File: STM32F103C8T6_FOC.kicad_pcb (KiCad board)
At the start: 4 copper layers, 42.3 x 42.3 mm, 80 parts, among them IC1 BD9E303EFJ-LBE2, IC2 AS5600-ASOT, J1 USB_C_Receptacle_USB2.0_16P, J2 Conn_01x02_Socket, J3 Conn_01x04_Pin, J4 Conn_01x02_Socket, J5 Conn_01x04_Pin, J6 Conn_01x02_Socket, U2 SN65HVD230DR, U3 USBLC6-2SC6, U4 M24C64-RMN6TP, U5 TMC2209-LA, Y1 Crystal_16MHz

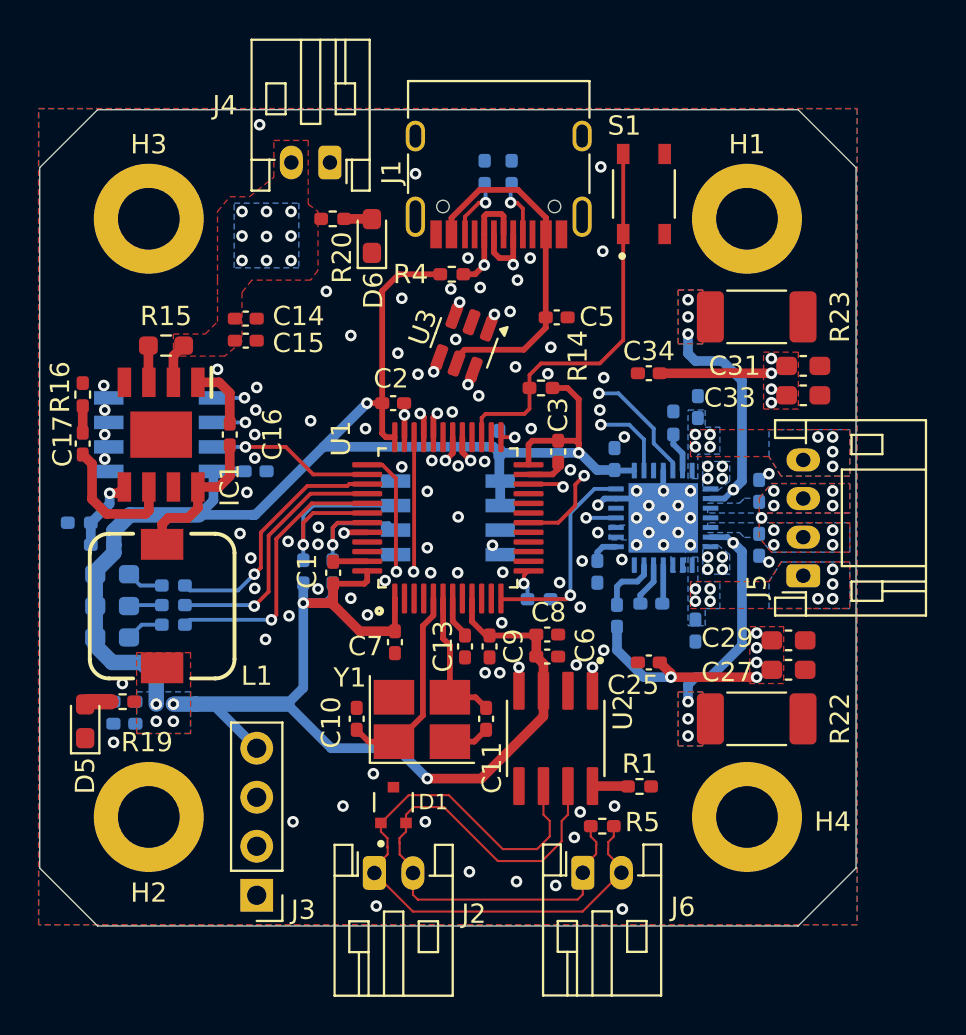
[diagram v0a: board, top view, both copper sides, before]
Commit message: Schematic check, Text adjustment & QoL changes
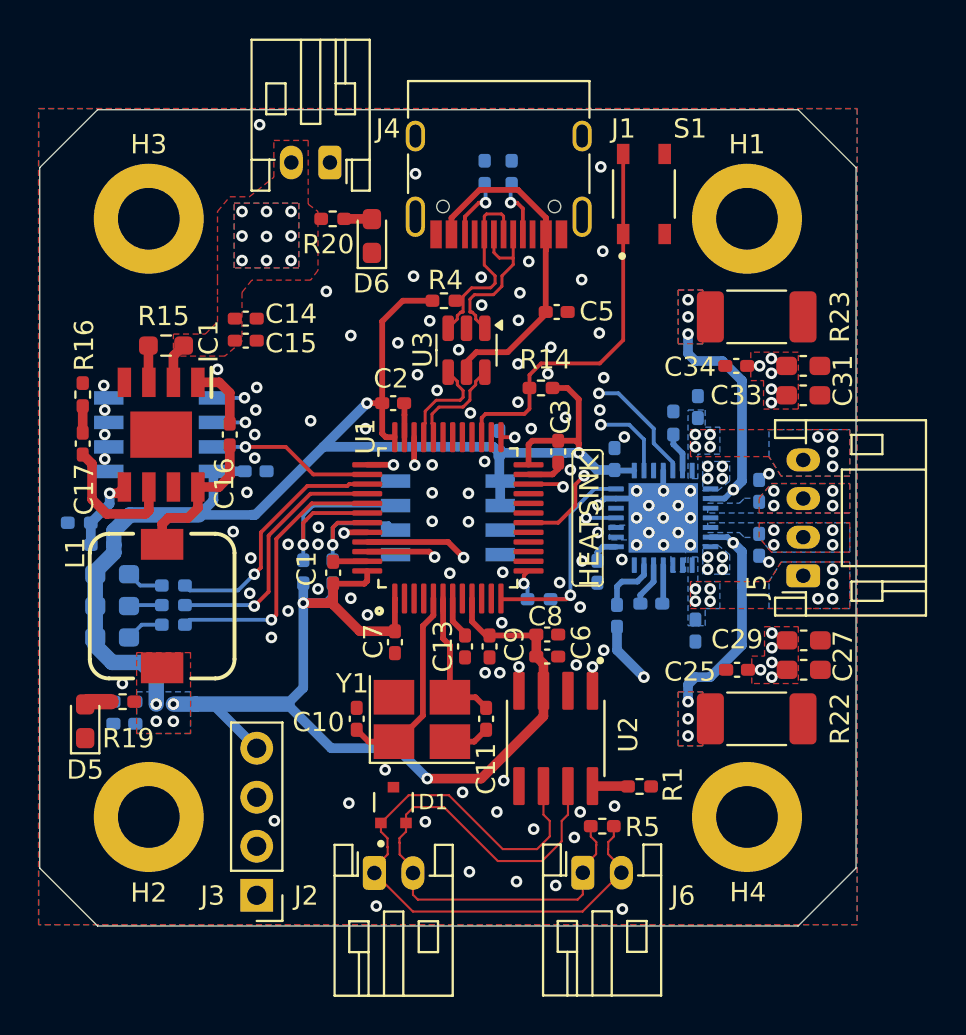
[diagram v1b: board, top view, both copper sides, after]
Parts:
- C27, C29, C31, C33: value 10uF -> 47uF
- moved C25 4.59 mm to (167.5, 108.2)
- moved C34 4.55 mm to (167.5, 92.5)
- moved R4 1.43 mm to (152.3, 89.1)
- moved C27 0.79 mm to (171.0, 108.2)
- moved C29 0.79 mm to (171.0, 106.7)
- moved U3 0.40 mm to (153.5, 91.6), turned to -90 degrees
- moved C5 0.28 mm to (158.2, 89.7)
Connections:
- U1 pad 29: /CAN_TX -> unconnected-(U1-PA8-Pad29)
- U1 pad 30: /CAN_RX -> unconnected-(U1-PA9-Pad30)
- U1 pad 45: unconnected-(U1-PB8-Pad45) -> /CAN_TX
- U1 pad 46: unconnected-(U1-PB9-Pad46) -> /CAN_RX
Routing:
- net +12V: track 77.7 -> 65.1 mm, vias 26 -> 28
- net /CAN_TX: track 18.7 -> 16.2 mm
- net /CAN_RX: track 15.8 -> 13.6 mm
- net +3.3V: track 126.6 -> 124.7 mm
- net /MCU_Peripherals/USB2_D-: track 7.46 -> 8.82 mm, vias 2 -> 0
- net /MCU_Peripherals/USB2_D+: track 10.4 -> 9.73 mm, vias 2 -> 0
- net /USB0_D+: track 4.63 -> 5.26 mm, vias 2 -> 0
- net Net-(U3-VBUS): track 18.2 -> 17.6 mm
- net /USB0_D-: track 5.40 -> 5.26 mm, vias 2 -> 0
- net GND: vias 104 -> 105
- added copper zone on In2.Cu, net +12V
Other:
- board text added: "3.3V"
- board text added: "B2 B1 A1 A2"
- board text added: "CLK"
- board text added: "DIO"
- board text added: "GND"
- board text added: "GND 12V"
- board text added: "H-L"
- board text added: "HEATSINK"
- board text added: "JLCJLCJLCJLC"
- board text added: "L-H"

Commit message: Constrains & Check
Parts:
- C10, C11: value C -> 30pF; footprint Capacitor_SMD:C_0402_1005Metric_Pad0.74x0.62mm_HandSolder -> Capacitor_SMD:C_0603_1608Metric_Pad1.08x0.95mm_HandSolder
- C14, C15, C16, C17, C18, C19: footprint Capacitor_SMD:C_0402_1005Metric_Pad0.74x0.62mm_HandSolder -> Capacitor_SMD:C_0603_1608Metric_Pad1.08x0.95mm_HandSolder
- R16, R17, R18: footprint Resistor_SMD:R_0402_1005Metric_Pad0.72x0.64mm_HandSolder -> Resistor_SMD:R_0603_1608Metric_Pad0.98x0.95mm_HandSolder
- moved R4 2.01 mm to (153.5, 87.4)
- moved R18 1.22 mm to (133.4, 99.4), turned to 90 degrees
- moved C14 0.91 mm to (142.8, 89.6)
- moved R16 0.87 mm to (133.2, 93.2)
- moved C15 0.78 mm to (142.8, 91.0)
- moved C10 0.70 mm to (147.1, 110.6)
- moved C18 0.58 mm to (135.3, 111.3)
- moved C19 0.53 mm to (135.2, 109.8)
- moved Y1 0.46 mm to (150.7, 110.8)
- moved C17 0.41 mm to (133.2, 96.5)
- moved R17 0.28 mm to (134.3, 101.7)
- moved C11 0.26 mm to (154.3, 110.6)
- moved C16 0.08 mm to (141.1, 96.0)
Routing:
- net +12V: track 65.1 -> 62.0 mm
- net GND: track 15.3 -> 13.1 mm, vias 105 -> 98
- net +3.3V: track 124.7 -> 126.5 mm
- net /MCU_Peripherals/USB2_D+: track 9.73 -> 8.62 mm
- net /MCU_Peripherals/CAN_N: track 33.8 -> 33.1 mm
- net /MCU_Peripherals/USB2_D-: track 8.82 -> 8.15 mm
- net Net-(IC1-FB): track 3.97 -> 4.61 mm
